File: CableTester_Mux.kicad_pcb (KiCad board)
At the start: 2 copper layers, 52.1 x 66 mm, 75 parts, among them J1 MircoMatch, J2 MircoMatch, J3 MircoMatch, J4 MircoMatch, J5 1787072, J6 SMB, J7 Keystone 7792, J8 Keystone 7792, U1 DG1206EUI+

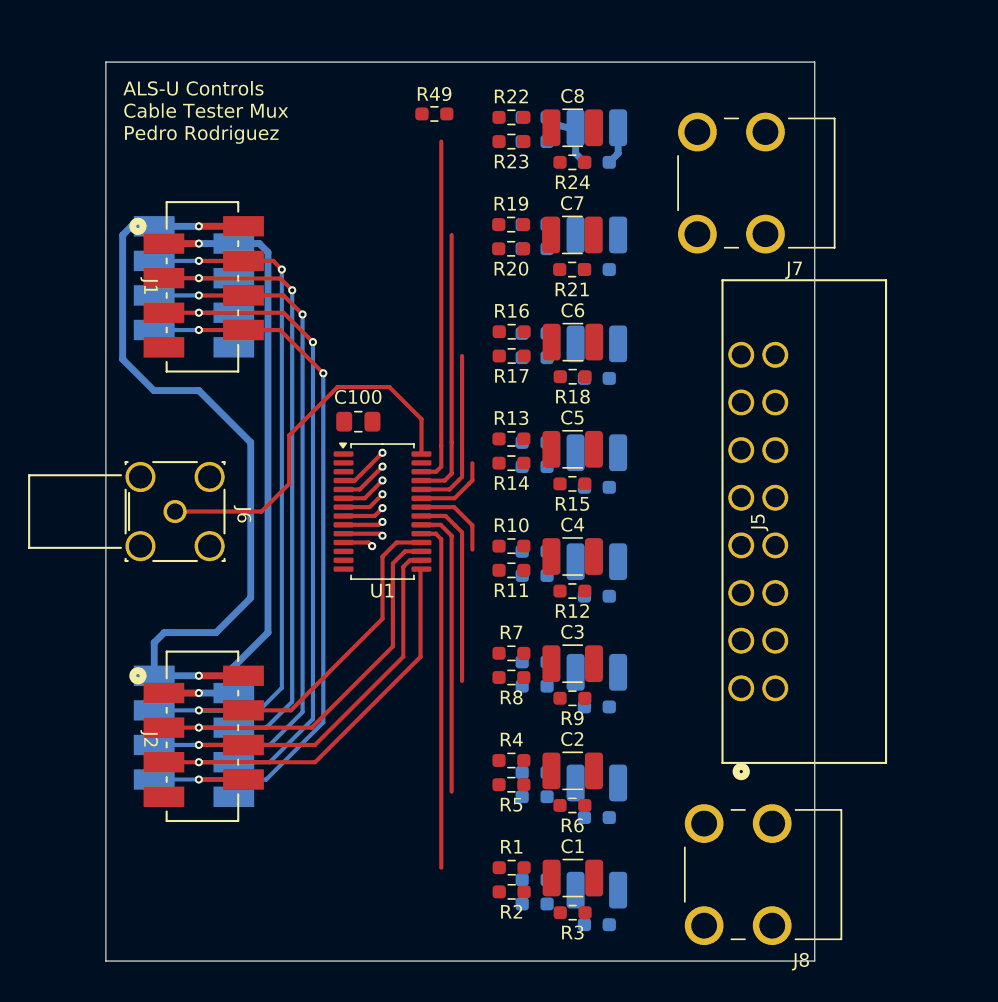
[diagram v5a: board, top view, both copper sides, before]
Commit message: Removed DC-Blocking filter and update schmatic and layout
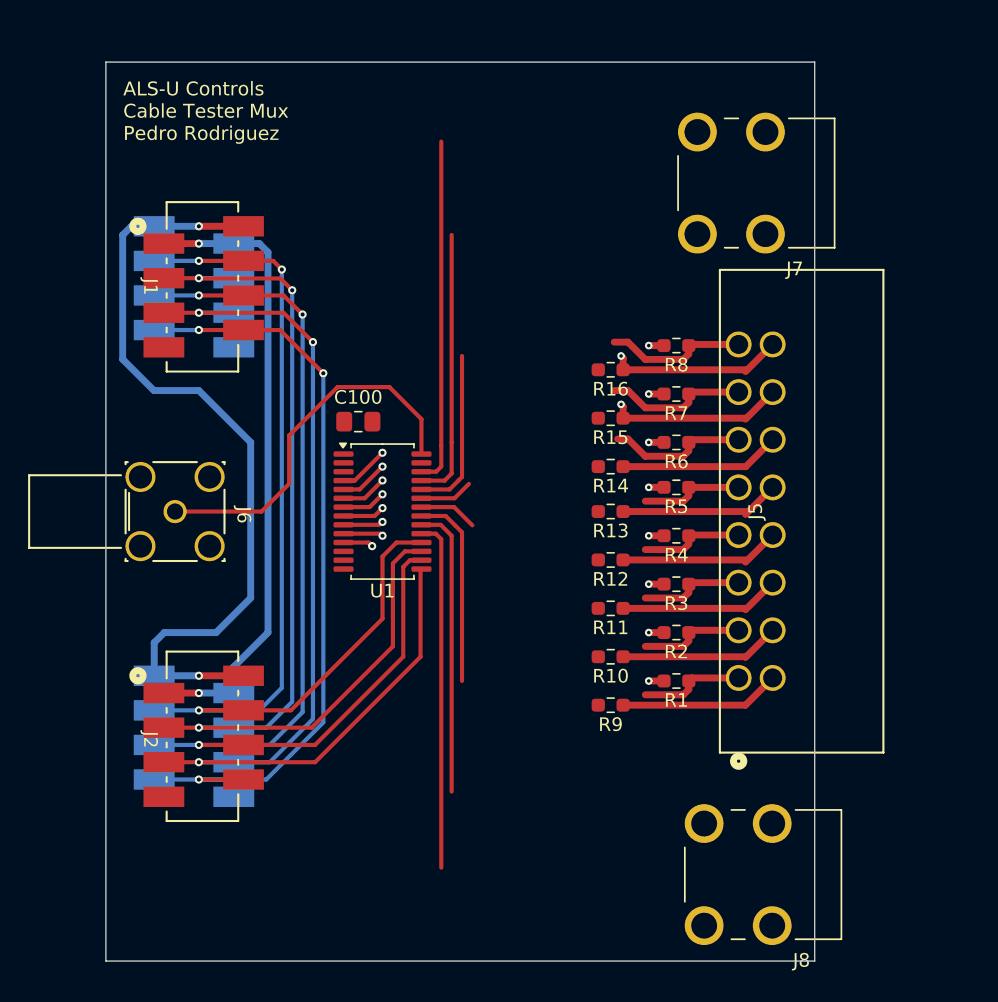
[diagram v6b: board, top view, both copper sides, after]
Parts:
- removed C1, C10, C11, C12, C13, C14, C15, C16, C2, C3, C4, C5, C6, C7, C8, C9: 10uF, Capacitor_SMD:C_1210_3225Metric_Pad1.33x2.70mm_HandSolder
- removed R17, R19, R20, R22, R23, R25, R26, R28, R29, R31, R32, R34, R35, R37, R38, R40, R41, R43, R44, R46, R47: 100k, Resistor_SMD:R_0603_1608Metric_Pad0.98x0.95mm_HandSolder
- removed R18, R21, R24, R27, R30, R33, R36, R39, R42, R45, R48, R49: 0R, Resistor_SMD:R_0603_1608Metric_Pad0.98x0.95mm_HandSolder
- R1, R10, R11, R13, R14, R16, R2, R4, R5, R7, R8: value 100k -> 1M
- R12, R15, R3, R6, R9: value 0R -> 1M
- moved R6 27.7 mm to (171.9, 91.9), turned to 180 degrees
- moved R8 27.2 mm to (171.9, 84.8)
- moved R3 25.3 mm to (171.9, 102.3), turned to 180 degrees
- moved R5 25.0 mm to (171.9, 95.2)
- moved R7 22.6 mm to (171.9, 88.3), turned to 180 degrees
- moved R2 22.6 mm to (171.9, 105.9)
- moved R4 20.5 mm to (171.9, 98.8), turned to 180 degrees
- moved R1 18.3 mm to (171.9, 109.4), turned to 180 degrees
- moved R10 10.9 mm to (167.1, 107.6), turned to 180 degrees
- moved R13 9.04 mm to (167.1, 97.0), turned to 180 degrees
- moved R11 7.81 mm to (167.1, 104.1)
- moved R16 7.79 mm to (167.1, 86.6), turned to 180 degrees
- moved R14 7.30 mm to (167.1, 93.7)
- moved R15 5.59 mm to (167.1, 90.1), turned to 180 degrees
- moved R12 3.62 mm to (167.1, 100.5), turned to 180 degrees
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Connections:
- J5 pad 1: /Jack1 -> /Mux1
- J5 pad 10: /Jack10 -> /Mux10
- J5 pad 11: /Jack11 -> /Mux11
- J5 pad 12: /Jack12 -> /Mux12
- J5 pad 13: /Jack13 -> /Mux13
- J5 pad 14: /Jack14 -> /Mux14
- J5 pad 15: /Jack15 -> /Mux15
- J5 pad 16: /Jack16 -> /Mux16
- J5 pad 2: /Jack2 -> /Mux2
- J5 pad 3: /Jack3 -> /Mux3
- J5 pad 4: /Jack4 -> /Mux4
- J5 pad 5: /Jack5 -> /Mux5
- J5 pad 6: /Jack6 -> /Mux6
- J5 pad 7: /Jack7 -> /Mux7
- J5 pad 8: /Jack8 -> /Mux8
- J5 pad 9: /Jack9 -> /Mux9
- R1 pad 1: /Filter1/DC_BIAS -> /Mux1
- R1 pad 2: /Mux1 -> GND
- R10 pad 1: /Filter1/DC_BIAS -> /Mux10
- R10 pad 2: /Mux4 -> GND
- R11 pad 1: /Mux4 -> /Mux11
- R12 pad 1: /Mux4 -> /Mux12
- R12 pad 2: /Jack4 -> GND
- R13 pad 1: /Filter1/DC_BIAS -> /Mux13
- R13 pad 2: /Mux5 -> GND
- R14 pad 1: /Mux5 -> /Mux14
- R15 pad 1: /Mux5 -> /Mux15
- R15 pad 2: /Jack5 -> GND
- R16 pad 1: /Filter1/DC_BIAS -> /Mux16
- R16 pad 2: /Mux6 -> GND
- R2 pad 1: /Mux1 -> /Mux2
- R3 pad 1: /Mux1 -> /Mux3
- R3 pad 2: /Jack1 -> GND
- R4 pad 1: /Filter1/DC_BIAS -> /Mux4
- R4 pad 2: /Mux2 -> GND
- R5 pad 1: /Mux2 -> /Mux5
- R6 pad 1: /Mux2 -> /Mux6
- R6 pad 2: /Jack2 -> GND
- R7 pad 1: /Filter1/DC_BIAS -> /Mux7
- R7 pad 2: /Mux3 -> GND
- R8 pad 1: /Mux3 -> /Mux8
- R9 pad 1: /Mux3 -> /Mux9
- R9 pad 2: /Jack3 -> GND
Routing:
- net /Mux15: track 3.56 -> 16.4 mm, vias 1 -> 2
- net /Mux9: track 2.21 -> 14.0 mm
- net /Mux12: track 3.10 -> 14.9 mm
- net /Mux11: track 2.95 -> 14.8 mm
- net /Mux10: track 2.93 -> 14.7 mm
- net /Mux14: track 3.41 -> 15.2 mm
- net /Mux13: track 3.37 -> 15.2 mm
- net /Mux7: track 20.0 -> 30.5 mm
- net /Mux8: track 25.5 -> 36.0 mm
- net /Mux6: track 12.2 -> 22.5 mm
- net GND: track 0.00 -> 8.96 mm, vias 0 -> 8
- net /Mux1: track 25.8 -> 33.5 mm
- net /Mux2: track 21.3 -> 29.1 mm
- net /Mux3: track 14.4 -> 22.1 mm
- net /Mux16: track 10.6 -> 16.6 mm, vias 1 -> 2
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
